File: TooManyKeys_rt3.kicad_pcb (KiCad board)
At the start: 6 copper layers, 156 x 116.5 mm, 89 parts, among them U1 TLV61070ADBV, U2 SN74LV1T126DBVR

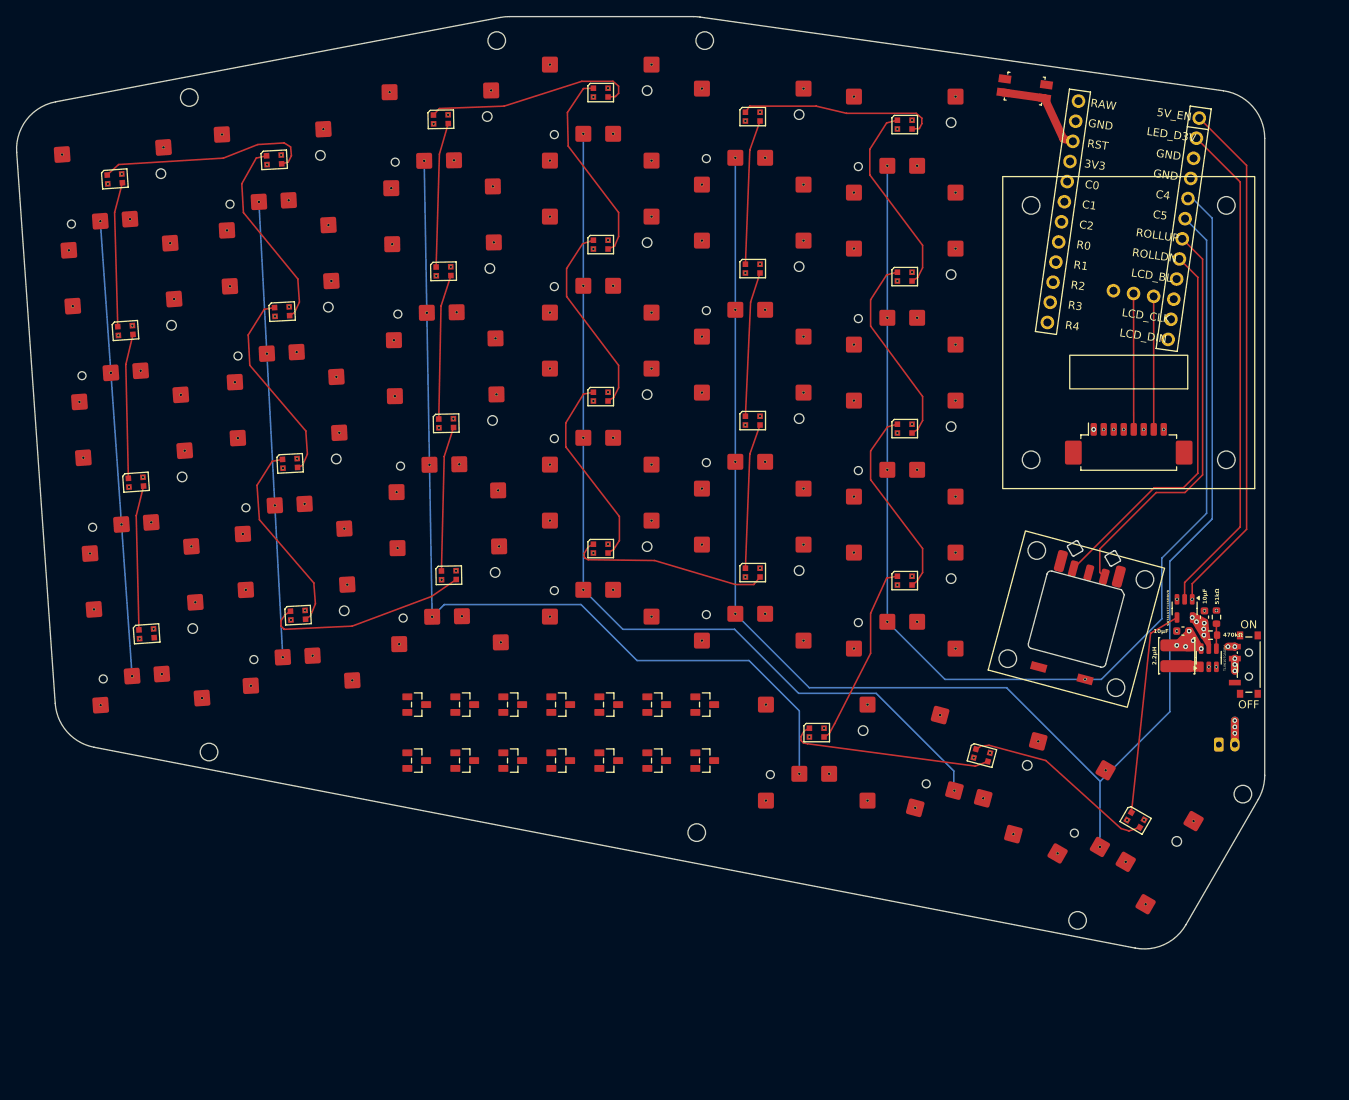
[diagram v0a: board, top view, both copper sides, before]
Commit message: Finish clean routing. Attempted sync of schematic failed, but board LGTM and passes DRC other than CKW12 edge issues of no concern.
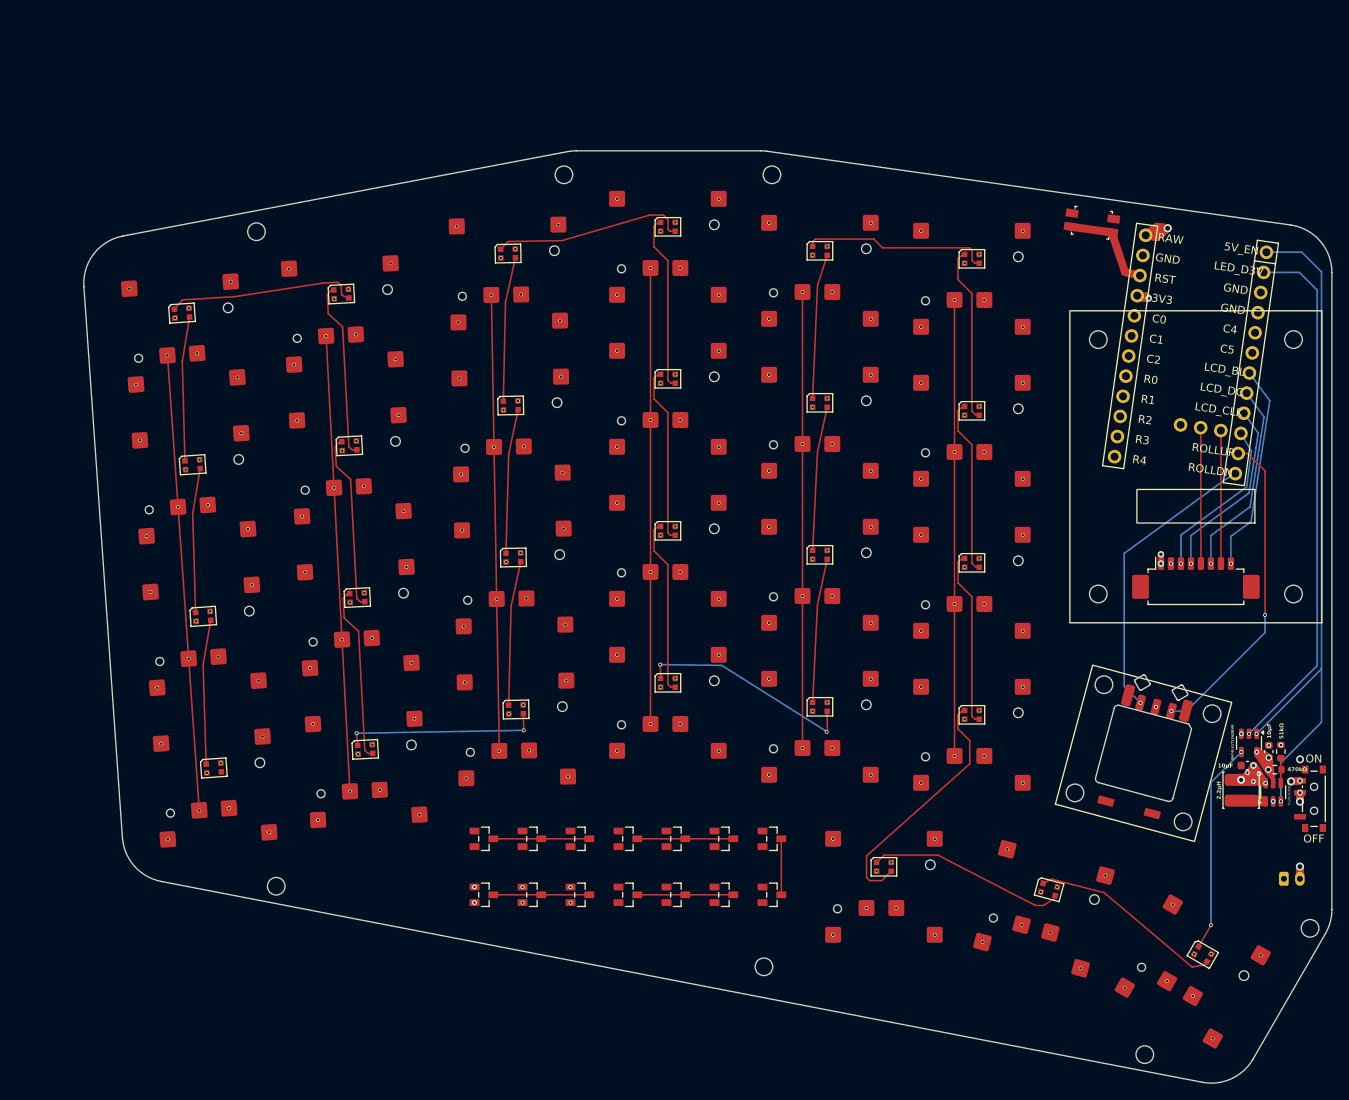
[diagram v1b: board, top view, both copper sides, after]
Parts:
- moved D14 18.8 mm to (138.7, 190.2)
- moved S20 18.8 mm to (144.7, 112.2)
- moved MCU1 18.8 mm to (191.2, 121.4)
- moved S22 18.8 mm to (163.7, 151.2)
- moved CONN1 18.8 mm to (191.7, 151.2)
- moved MH5 18.8 mm to (137.7, 199.2)
- moved D3 18.8 mm to (114.7, 190.2)
- moved D10 18.8 mm to (120.7, 183.2)
- moved S9 18.8 mm to (106.7, 169.5)
- moved LED14 18.8 mm to (125.7, 144.7)
- moved S21 18.8 mm to (163.7, 170.2)
- moved LED12 18.8 mm to (105.7, 110.0)
- moved LED16 18.8 mm to (125.7, 106.7)
- moved LED26 18.8 mm to (173.3, 189.5)
- moved MH7 18.8 mm to (205.9, 194.4)
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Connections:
- D1 pad 1: finger_pinky_num -> finger_outer_num
- D1 pad 2: finger_outer_num -> finger_pinky_num
- D12 pad 1: finger_inner_bottom -> finger_index_bottom
- D12 pad 2: finger_index_bottom -> finger_inner_bottom
- D2 pad 1: finger_middle_num -> finger_ring_num
- D2 pad 2: finger_ring_num -> finger_middle_num
- D3 pad 1: finger_inner_num -> finger_index_num
- D3 pad 2: finger_index_num -> finger_inner_num
- D5 pad 1: finger_middle_top -> finger_ring_top
- D5 pad 2: finger_ring_top -> finger_middle_top
- D6 pad 1: finger_inner_top -> finger_index_top
- D6 pad 2: finger_index_top -> finger_inner_top
- D8 pad 1: finger_middle_home -> finger_ring_home
- D8 pad 2: finger_ring_home -> finger_middle_home
- D9 pad 1: finger_inner_home -> finger_index_home
- D9 pad 2: finger_index_home -> finger_inner_home
- MCU1 pad 10: LCD_DC -> LCD_DIN
- MCU1 pad 11: LCD_CLK -> ROLLUP
- MCU1 pad 12: LCD_DIN -> ROLLDN
- MCU1 pad 7: ROLLUP -> LCD_BL
- MCU1 pad 8: ROLLDN -> LCD_DC
- MCU1 pad 9: LCD_BL -> LCD_CLK
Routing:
- net finger_inner_num: track 0.00 -> 246.2 mm, vias 0 -> 1
- net finger_index_num: track 0.00 -> 225.7 mm, vias 0 -> 1
- net finger_middle_num: track 0.00 -> 197.3 mm, vias 0 -> 1
- net finger_ring_num: track 0.00 -> 169.7 mm, vias 0 -> 1
- net RAW: track 108.8 -> 264.4 mm, vias 7 -> 10
- net C3: track 202.2 -> 57.0 mm
- net C4: track 199.7 -> 57.0 mm
- net finger_pinky_num: track 0.00 -> 140.8 mm, vias 0 -> 1
- net finger_outer_num: track 0.00 -> 118.2 mm, vias 0 -> 1
- net C5: track 150.9 -> 57.0 mm, vias 1 -> 0
- net C2: track 116.9 -> 57.0 mm
- net 3V3: track 35.2 -> 79.8 mm, vias 1 -> 3
- net 5V_EN: track 75.5 -> 87.7 mm
- net R0: track 0.00 -> 12.0 mm
- net R1: track 0.00 -> 12.0 mm
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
